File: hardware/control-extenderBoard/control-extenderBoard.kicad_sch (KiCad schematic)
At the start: 72 parts, among them J1 SCL6 + GND (TP), J10 SCL6 + GND (TP), J11 SDA6 + GND (TP), J17 24V IN, J18 GND, J2 12V Out, J3 5V out, J4 SDA6 + GND (TP), J5 GND, J6 SCL7 Differential (TP), J7 SDA7 Differential (TP), J8 RS485, J9 3V3 out, P1 ISP, U1 MAX3485, U10 LM2576T-12, U2 PCA9600D, U3 TCA9548A_1-to-8_I2C_Multiplex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, U4 LM2576T-3.3, U5 PCA9600D, U6 PCA82C251, U7 PCA82C251, U8 PCA9600D, U9 LM2576T-5

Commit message: extenderBoard: Add gyro board, Optimize i2c-boost + filter, Update footprints
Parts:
- added D10, D7: BAT54A, Package_TO_SOT_SMD:SOT-23, symbol Diode:BAT54A
- added D11, D12, D8, D9: SMAJ150A, Diode_SMD:D_SMA, symbol Diode:SMAJ150A
- added D6: TVS 40V, Diode_THT:D_DO-201AE_P15.24mm_Horizontal, symbol Diode:1.5KExxCA
- added J12: 3V3 + GND (TP), terminals_libJonny:ScrewTerminal_P3.5mm_2Pin_FP7x7, symbol Connector:Screw_Terminal_01x02
- added J13: 12V + GND (TP), terminals_libJonny:ScrewTerminal_P3.5mm_2Pin_FP7x7, symbol Connector:Screw_Terminal_01x02
- added J14: SCL6 + GND (TP), terminals_libJonny:ScrewTerminal_P3.5mm_2Pin_FP7x7, symbol Connector:Screw_Terminal_01x02
- added J15: SDA6 + GND (TP), terminals_libJonny:ScrewTerminal_P3.5mm_2Pin_FP7x7, symbol Connector:Screw_Terminal_01x02
- added R25, R26: 2k2, Resistor_THT:R_Axial_DIN0207_L6.3mm_D2.5mm_P10.16mm_Horizontal, symbol Device:R
- added R27: 2.5, Resistor_THT:R_Axial_DIN0922_L20.0mm_D9.0mm_P25.40mm_Horizontal, symbol Device:R
- added TP1: 24V filtered, Connector_PinHeader_1.00mm:PinHeader_1x01_P1.00mm_Vertical, symbol Connector:TestPoint
- added U11: ICM-426XX_Breakout, modules_libJonny:ICM-426XX_6-Axis-Gyro_Breakout_Board, symbol modules_libJonny:ICM-426XX_Breakout
- F2: value F-Servo -> F-total-control-supply
- J1: value SCL6 + GND (TP) -> 12V + GND (TP); footprint Connector_Phoenix_MC:PhoenixContact_MC_1,5_2-GF-3.5_1x02_P3.50mm_Horizontal_ThreadedFlange_MountHole -> terminals_libJonny:ScrewTerminal_P3.5mm_2Pin_FP7x7
- J10, J11, J6, J7: footprint Connector_Phoenix_MC:PhoenixContact_MC_1,5_2-GF-3.5_1x02_P3.50mm_Horizontal_ThreadedFlange_MountHole -> terminals_libJonny:ScrewTerminal_P3.5mm_2Pin_FP7x7
- J4: value SDA6 + GND (TP) -> 3V3 + GND (TP); footprint Connector_Phoenix_MC:PhoenixContact_MC_1,5_2-GF-3.5_1x02_P3.50mm_Horizontal_ThreadedFlange_MountHole -> terminals_libJonny:ScrewTerminal_P3.5mm_2Pin_FP7x7
- R1: value 1k -> 2k2
- R23, R24, R4: value 1k -> 750
- R3: value 2k2 -> 750
- U1: footprint Package_SO:SOIC-8_3.9x4.9mm_P1.27mm -> modules_libJonny:Adapter-Board_SOP8_to_DIP8
- U6, U7: footprint Package_SO:SO-8_3.9x4.9mm_P1.27mm -> modules_libJonny:Adapter-Board_SOP8_to_DIP8
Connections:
- net +12V: now also J1.1 (Pin_1), R3.1, J13.1 (Pin_1); no longer R1.1
- net +24V filtered: now also C2.2, C3.2, C5.2, C6.2, C7.2, C8.2, D13.3 (common), D2.2 (A), D4.2 (A), D5.2 (A), J1.2 (Pin_2), J10.1 (Pin_1), J11.1 (Pin_1), J18.1 (Pin_1), J18.2 (Pin_2), J4.2 (Pin_2), J5.1 (Pin_1), J5.2 (Pin_2), J8.1 (Pin_1), R12.2, R37.2, R5.2, R6.2, R9.2, U1.5 (GND), U10.3 (GND), U10.5 (~{ON}/OFF), U2.4 (GND), U3.2 (GND), U3.6 (A0), U3.7 (A1), U3.8 (A2), U4.3 (GND), U4.5 (~{ON}/OFF), U5.4 (GND), U6.2 (GND), U7.2 (GND), U8.4 (GND), U9.3 (GND), U9.5 (~{ON}/OFF), D10.3, D11.2 (A2), D12.2 (A2), D6.1 (A1), D7.3, D8.2 (A2), D9.2 (A2), J12.2 (Pin_2), J13.2 (Pin_2), J14.1 (Pin_1), J15.1 (Pin_1), R27.2, TP1.1, U11.2 (GND); no longer C1.2, D1.1 (K), F2.1, TP6.1
- net +3V3: now also J4.1 (Pin_1), R1.1, J12.1 (Pin_1), R25.1, R26.1, U11.1 (VCC); no longer R3.1
- net I2C0_SCL: now also R25.2, U11.3 (SCL)
- net I2C0_SDA: now also R26.2, U11.4 (SDA)
- net I2C5_SCL: now also R2.2, U2.1 (SX)
- net I2C5_SDA: now also R1.2, U2.7 (SY)
- net I2C6_SCL: no longer R2.2, U2.1 (SX)
- net I2C6_SDA: no longer R3.2, U2.7 (SY)
- net at J11.2 (Pin_2), R24.2, U8.5 (TY)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: now also D7.1, D9.1 (A1)
- net at J10.2 (Pin_2), R23.2, U8.2 (RX)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: now also D7.2, D8.1 (A1)
- net at U2.5 (TY), U2.6 (RY): now also R4.2, D10.1, D11.1 (A1), J15.2 (Pin_2); no longer J4.2 (Pin_2), R1.2
- net at U2.2 (RX), U2.3 (TX): now also R3.2, D10.2, D12.1 (A1), J14.2 (Pin_2); no longer J1.2 (Pin_2), R4.2
- removed net GND: C2.2, C3.2, C5.2, C6.2, C7.2, C8.2, D13.3 (common), D2.2 (A), D4.2 (A), D5.2 (A), J1.1 (Pin_1), J10.1 (Pin_1), J11.1 (Pin_1), J18.1 (Pin_1), J18.2 (Pin_2), J4.1 (Pin_1), J5.1 (Pin_1), J5.2 (Pin_2), J8.1 (Pin_1), R12.2, R37.2, R5.2, R6.2, R9.2, U1.5 (GND), U10.3 (GND), U10.5 (~{ON}/OFF), U2.4 (GND), U3.2 (GND), U3.6 (A0), U3.7 (A1), U3.8 (A2), U4.3 (GND), U4.5 (~{ON}/OFF), U5.4 (GND), U6.2 (GND), U7.2 (GND), U8.4 (GND), U9.3 (GND), U9.5 (~{ON}/OFF)
- new net: D1.1 (K), D6.2 (A2), F2.1, R27.1, TP6.1
- new net GNDPWR: C1.2
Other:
- note added: "CAT6 cable control-extenderBoard -> I2C Sensor pcb Axle: - Twisted pair: GND + SCL - Twisted pair: GND + SDA - Twisted pair: GND + 12V (for pullup cable) - Twisted pair: GND + 3V3 (supply module)"
- note added: "ICM-42688 6-axis gyro module"
- moved on the sheet: C4, D1, D3, J10, J11, J6, J7, P1, R10, R11, R12, R13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

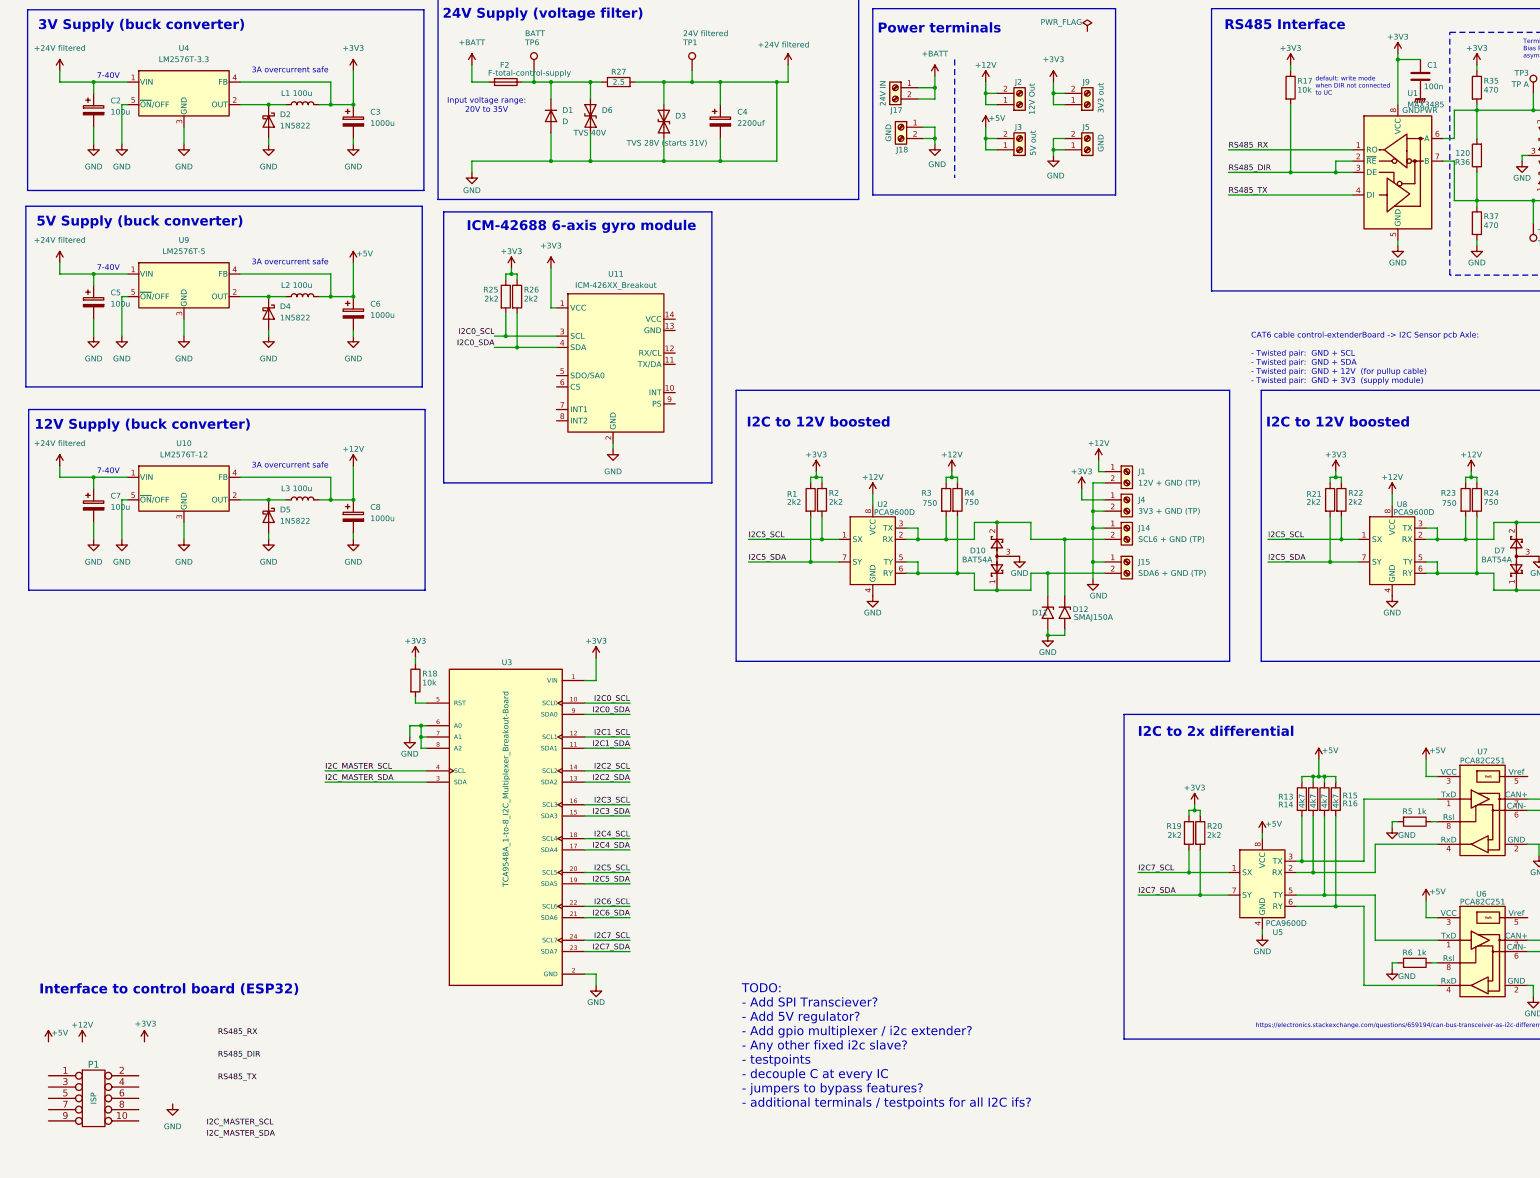
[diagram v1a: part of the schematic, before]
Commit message: extenderBoard: Add remote encoder board, start arranging
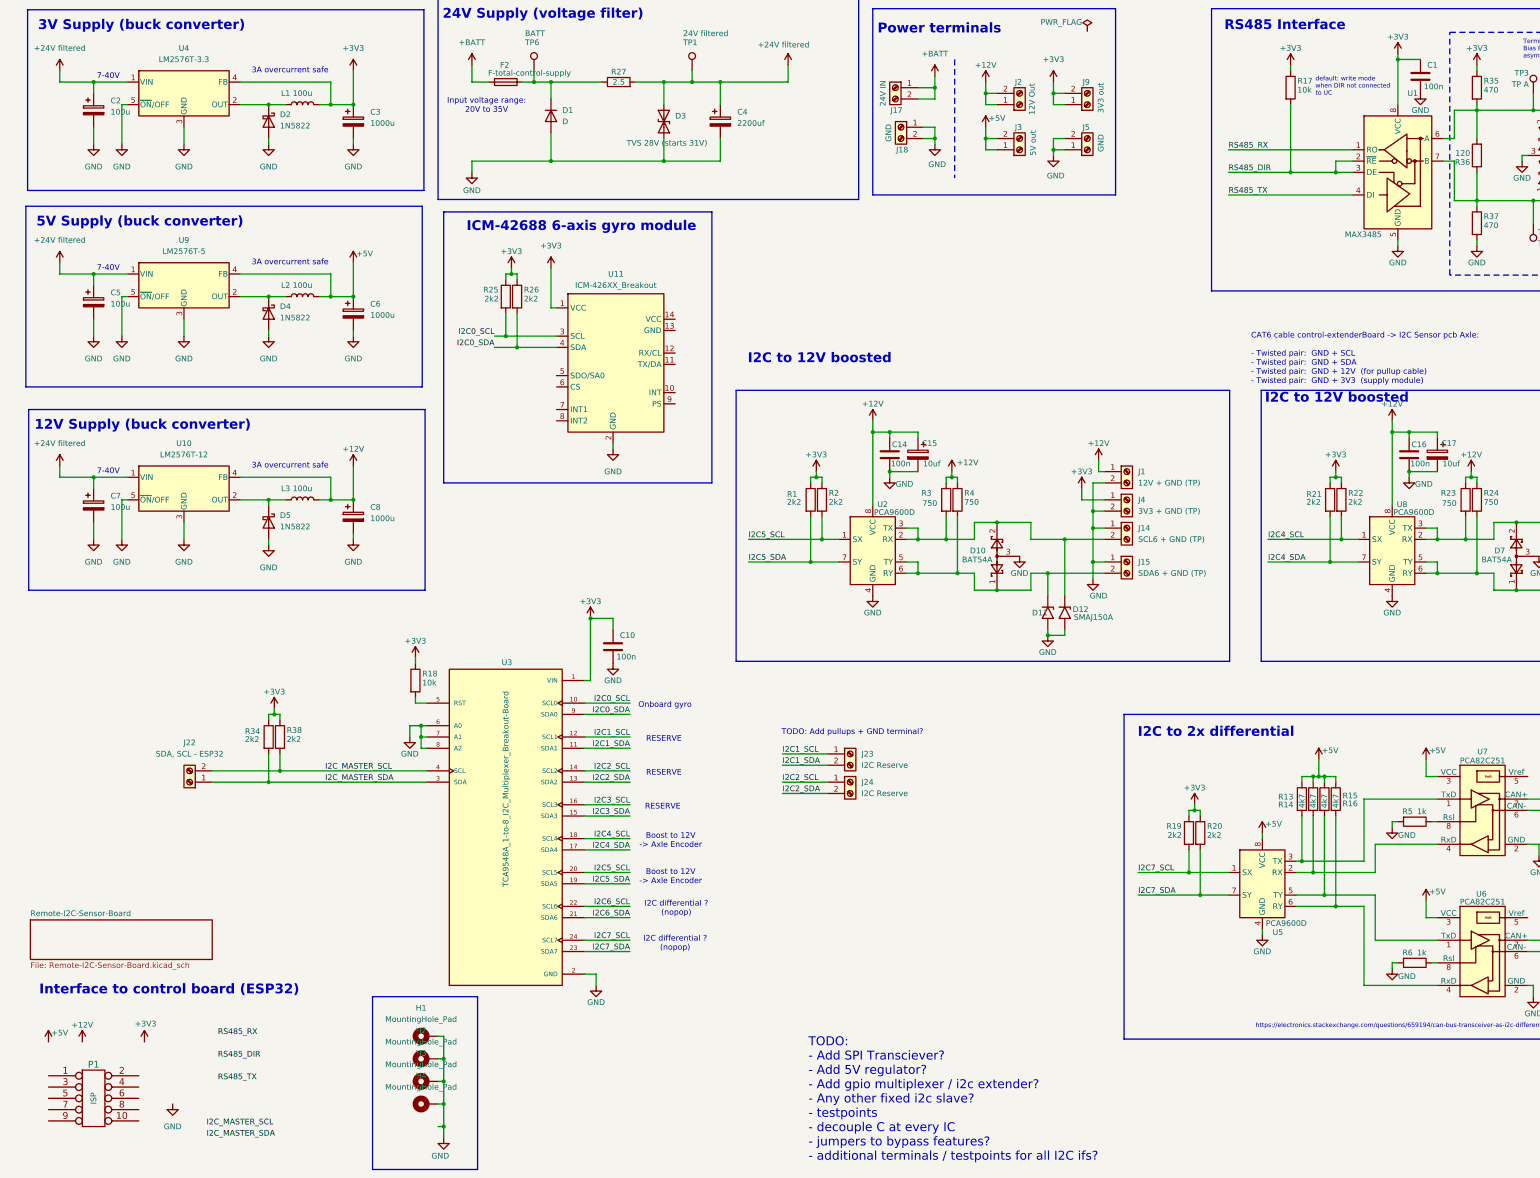
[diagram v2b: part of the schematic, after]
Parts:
- removed D6: TVS 40V, Diode_THT:D_DO-201AE_P15.24mm_Horizontal, symbol Diode:1.5KExxCA
- added C10, C14, C16: 100n, Capacitor_THT:C_Disc_D7.0mm_W2.5mm_P5.00mm, symbol Device:C
- added C15, C17: 10uf, Capacitor_THT:CP_Radial_D5.0mm_P2.50mm, symbol Device:C_Polarized
- added H1, H2, H3, H4: MountingHole_Pad, mountingHoles_libJonny:MountingHole_2.2mm_NPTH-with-pad_DRC-clearance-error, symbol Mechanical:MountingHole_Pad
- added J22: SDA, SCL - ESP32, terminals_libJonny:ScrewTerminal_P3.5mm_2Pin_FP7x7, symbol Connector:Screw_Terminal_01x02
- added J23, J24: I2C Reserve, terminals_libJonny:ScrewTerminal_P3.5mm_2Pin_FP7x7, symbol Connector:Screw_Terminal_01x02
- added R34, R38: 2k2, Resistor_THT:R_Axial_DIN0207_L6.3mm_D2.5mm_P10.16mm_Horizontal, symbol Device:R
- C4: footprint Capacitor_THT:CP_Radial_D18.0mm_P7.50mm -> Capacitor_THT:CP_Radial_D13.0mm_P5.00mm
- R27: footprint Resistor_THT:R_Axial_DIN0922_L20.0mm_D9.0mm_P25.40mm_Horizontal -> resistors_libJonny:Cement-Power-R_L22_W10_P23_Horizontal
- U10, U4, U9: footprint Package_TO_SOT_THT:TO-220-5_Vertical -> Package_TO_SOT_THT:TO-220-5_P3.4x3.7mm_StaggerOdd_Lead3.8mm_Vertical
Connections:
- net +12V: now also C14.1, C15.1, C16.1, C17.1
- net +24V filtered: no longer C2.2, C3.2, C4.2, C5.2, C6.2, C7.2, C8.2, D1.2 (A), D10.3, D11.2 (A2), D12.2 (A2), D13.3 (common), D2.2 (A), D3.1 (A1), D4.2 (A), D5.2 (A), D7.3, D8.2 (A2), D9.2 (A2), J1.2 (Pin_2), J10.1 (Pin_1), J11.1 (Pin_1), J12.2 (Pin_2), J13.2 (Pin_2), J14.1 (Pin_1), J15.1 (Pin_1), J18.1 (Pin_1), J18.2 (Pin_2), J4.2 (Pin_2), J5.1 (Pin_1), J5.2 (Pin_2), J8.1 (Pin_1), R12.2, R37.2, R5.2, R6.2, R9.2, U1.5 (GND), U10.3 (GND), U10.5 (~{ON}/OFF), U11.2 (GND), U2.4 (GND), U3.2 (GND), U3.6 (A0), U3.7 (A1), U3.8 (A2), U4.3 (GND), U4.5 (~{ON}/OFF), U5.4 (GND), U6.2 (GND), U7.2 (GND), U8.4 (GND), U9.3 (GND), U9.5 (~{ON}/OFF)
- net +3V3: now also C10.1, R34.1, R38.1
- net I2C1_SCL: now also J23.1 (Pin_1)
- net I2C1_SDA: now also J23.2 (Pin_2)
- net I2C2_SCL: now also J24.1 (Pin_1)
- net I2C2_SDA: now also J24.2 (Pin_2)
- net I2C4_SCL: now also R22.2, U8.1 (SX)
- net I2C4_SDA: now also R21.2, U8.7 (SY)
- net I2C5_SCL: no longer R22.2, U8.1 (SX)
- net I2C5_SDA: no longer R21.2, U8.7 (SY)
- net I2C_MASTER_SCL: now also J22.2 (Pin_2), R38.2
- net I2C_MASTER_SDA: now also J22.1 (Pin_1), R34.2
- net GNDPWR renamed GND
- net GND: now also C2.2, C3.2, C4.2, C5.2, C6.2, C7.2, C8.2, D1.2 (A), D10.3, D11.2 (A2), D12.2 (A2), D13.3 (common), D2.2 (A), D3.1 (A1), D4.2 (A), D5.2 (A), D7.3, D8.2 (A2), D9.2 (A2), J1.2 (Pin_2), J10.1 (Pin_1), J11.1 (Pin_1), J12.2 (Pin_2), J13.2 (Pin_2), J14.1 (Pin_1), J15.1 (Pin_1), J18.1 (Pin_1), J18.2 (Pin_2), J4.2 (Pin_2), J5.1 (Pin_1), J5.2 (Pin_2), J8.1 (Pin_1), R12.2, R37.2, R5.2, R6.2, R9.2, U1.5 (GND), U10.3 (GND), U10.5 (~{ON}/OFF), U11.2 (GND), U2.4 (GND), U3.2 (GND), U3.6 (A0), U3.7 (A1), U3.8 (A2), U4.3 (GND), U4.5 (~{ON}/OFF), U5.4 (GND), U6.2 (GND), U7.2 (GND), U8.4 (GND), U9.3 (GND), U9.5 (~{ON}/OFF), C10.2, C14.2, C15.2, C16.2, C17.2, H1.1, H2.1, H3.1, H4.1
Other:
- added sheet Remote-I2C-Sensor-Board (Remote-I2C-Sensor-Board.kicad_sch)
- note added: "Boost to 12V -> Axle Encoder"
- note added: "I2C differential ? (nopop)"
- note added: "Onboard gyro"
- note added: "RESERVE"
- note added: "TODO: Add pullups + GND terminal?"
- moved on the sheet: D5

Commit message: extenderBoard: Evaluate part availability, Rework i2c protection
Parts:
- removed D10, D7: BAT54A, Package_TO_SOT_SMD:SOT-23, symbol Diode:BAT54A
- added D10, D19, D21, D22, D23, D24, D25, D7: BAS70-04, Package_TO_SOT_SMD:SOT-23-3, symbol Diode:BAT54SW
- added D17, D18, D20, D6: AQ4020-01FTG, Diode_SMD:D_SOD-323_HandSoldering, symbol Diode:SMAJ150A
- added J25, J26: I2C Reserve SDA/GND, terminals_libJonny:ScrewTerminal_P3.5mm_2Pin_FP7x7, symbol Connector:Screw_Terminal_01x02
- added R39, R40, R41, R42: 2k2, Resistor_THT:R_Axial_DIN0207_L6.3mm_D2.5mm_P10.16mm_Horizontal, symbol Device:R
- D11, D12, D8, D9: value SMAJ150A -> SMF12VTR; footprint Diode_SMD:D_SMA -> Diode_SMD:D_SOD-123F
- J23, J24: value I2C Reserve -> I2C Reserve SCL/GND
- L1: value 100u -> 150u; footprint Inductor_THT:L_Radial_D8.7mm_P5.00mm_Fastron_07HCP -> Inductor_THT:L_Radial_D12.5mm_P7.00mm_Fastron_09HCP
- L2: value 100u -> 330u; footprint Inductor_THT:L_Radial_D8.7mm_P5.00mm_Fastron_07HCP -> Inductor_THT:L_Radial_D10.5mm_P5.00mm_Abacron_AISR-01
- L3: value 100u -> 470u; footprint Inductor_THT:L_Radial_D8.7mm_P5.00mm_Fastron_07HCP -> Inductor_THT:L_Toroid_Vertical_L21.6mm_W11.4mm_P7.62mm_Pulse_KM-3
- renumbered U11 to a1
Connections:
- net +12V: now also D10.2 (K), D21.2 (K), D22.2 (K), D7.2 (K)
- net +3V3: now also D19.2 (K), D23.2 (K), D24.2 (K), D25.2 (K), R39.1, R40.1, R41.1, R42.1
- net GND: now also J23.2 (Pin_2), J24.2 (Pin_2), D10.1 (A), D17.2 (A2), D18.2 (A2), D19.1 (A), D20.2 (A2), D21.1 (A), D22.1 (A), D23.1 (A), D24.1 (A), D25.1 (A), D6.2 (A2), D7.1 (A), J25.2 (Pin_2), J26.2 (Pin_2)
- net I2C1_SCL: now also D18.1 (A1), D23.3 (COM), R39.2
- net I2C1_SDA: now also D19.3 (COM), D6.1 (A1), J25.1 (Pin_1), R40.2; no longer J23.2 (Pin_2)
- net I2C2_SCL: now also D17.1 (A1), D25.3 (COM), R41.2
- net I2C2_SDA: now also D20.1 (A1), D24.3 (COM), J26.1 (Pin_1), R42.2; no longer J24.2 (Pin_2)
- net SCL_Boost1: now reaches D12.1 (A1), J14.2 (Pin_2), R3.2, U2.2 (RX), U2.3 (TX)
- net SCL_Boost1: now also D22.3 (COM)
- net SDA_Boost1: now reaches D11.1 (A1), J15.2 (Pin_2), R4.2, U2.5 (TY), U2.6 (RY)
- net SDA_Boost1: now also D21.3 (COM)
- net SDA_Boost2: now reaches D9.1 (A1), J11.2 (Pin_2), R24.2, U8.5 (TY), U8.6 (RY)
- net SDA_Boost2: now also D7.3 (COM)
- net SCL_Boost2: now reaches D8.1 (A1), J10.2 (Pin_2), R23.2, U8.2 (RX), U8.3 (TX)
- net SCL_Boost2: now also D10.3 (COM)
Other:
- note added: "150uH picked for ~2A max out current"
- note added: "2x TVS spikes+ESD protection"
- note added: "330uH picked for ~1A max out current"
- note added: "470uH picked for ~1.3A max out current"
- note added: "Direct I2C (Reserve)"
- note added: "I2C boosted to 12V (Encoder 1)"
- note added: "I2C boosted to 12V (Encoder 2)"
- note added: "I2C to 2x differential (nopop)"
- note added: "RS485 Interface (nopop)"
- note added: "Separate PCB with i2c slave i2c magnetic encoder mounted at axle (see subsheet)"
- note added: "TODO: - Add SPI Transciever? - Add 5V regulator? - Add gpio multiplexer / i2c extender? - Any other fixed i2c slave? - testpoints - decouple C at every IC - jumpers to bypass features? - additional terminals / testpoints for all I2C ifs? - Additional large terminal for connecting Shield of cat6 cables -> frame? - protection i2c -> esp32 board as well? (diodes)"
- note added: "TODO: - jumper to select 5V or 3v3 pullup - 3V3, 5V terminals"
- note added: "TODO: GND terminal?"
- note added: "schottky array clamp to GND / 12V"
- note added: "schottky array clamp to GND / 3V3"
- note removed: "I2C to 12V boosted"
- note removed: "I2C to 2x differential"
- note removed: "RS485 Interface"
- note removed: "TODO: - Add SPI Transciever? - Add 5V regulator? - Add gpio multiplexer / i2c extender? - Any other fixed i2c slave? - testpoints - decouple C at every IC - jumpers to bypass features? - additional terminals / testpoints for all I2C ifs?"
- note removed: "TODO: Add pullups + GND terminal?"
- moved on the sheet: C1, C10, C14, C15, C16, C17, C2, C3, C4, C5, C6, C7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
